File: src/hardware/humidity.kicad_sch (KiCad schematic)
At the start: 2 parts

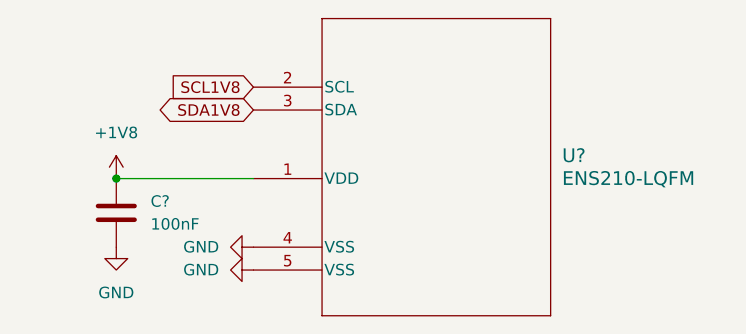
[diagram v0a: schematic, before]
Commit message: Added I²C Addresses
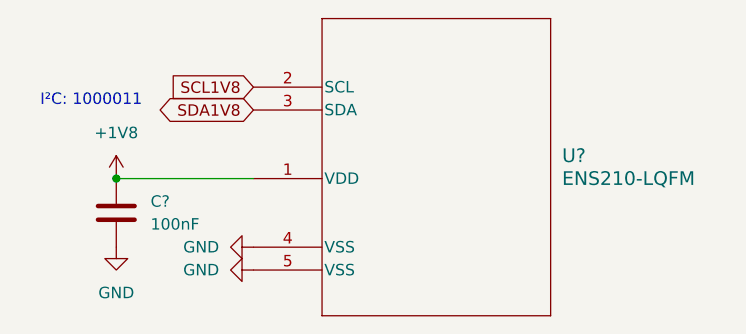
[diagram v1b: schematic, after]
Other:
- note added: "I²C: 1000011"
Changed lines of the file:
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@@
 		(date "2026-10-21")
+	)
+	(text "I²C: 1000011"
+		(exclude_from_sim no)
+		(at 116.586 95.504 0)
+		(effects
+			(font
+				(size 1.27 1.27)
+			)
+		)
 	)
 	(junction

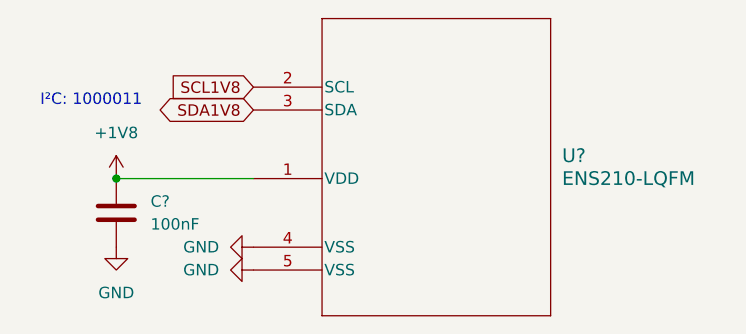
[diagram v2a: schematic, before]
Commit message: Replaced schematics, 3d models and footprints. Added vibration motor.
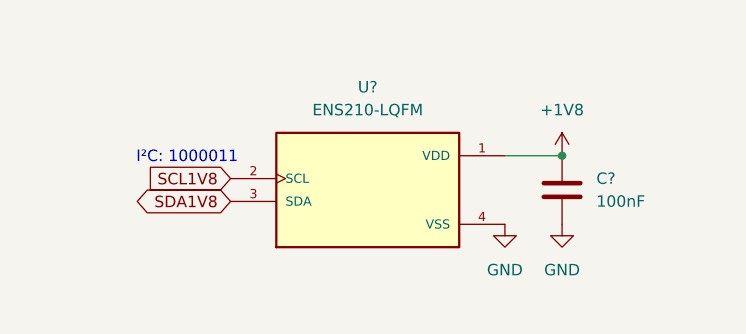
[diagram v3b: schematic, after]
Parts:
- removed U?: ENS210-LQFM, SON-04-ENS210_2X2_AMS, symbol ENS210-LQFM:ENS210-LQFM
- added U?: ENS210-LQFM, ENS210-LQFM:XDCR_ENS210-LQFM, symbol ENS210-LQFM:ENS210-LQFM
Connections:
- net +1V8: now also U?.1 (VDD)
- net GND: now also U?.4 (VSS), U?.5 (VSS)
- net SCL1V8: now also U?.2 (SCL)
- net SDA1V8: now also U?.3 (SDA)
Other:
- moved on the sheet: C?

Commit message: Cleanup & Fixes; Added footprints; Removed Light sensors
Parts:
- C56: renamed from C?; footprint (none) -> Capacitor_SMD:C_0603_1608Metric
- U18: renamed from U?; footprint ENS210-LQFM:XDCR_ENS210-LQFM -> Project:XDCR_ENS210-LQFM
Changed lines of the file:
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@@
 		(dnp no)
 		(fields_autoplaced yes)
-		(property "Reference" "#PWR0309"
+		(property "Reference" "#PWR0316"
 			(at 168.91 105.41 0)
 			(effects
@@
 			(project "raywatch"
 				(path "/7b654ee8-2a53-4d39-8b7d-32c7bb3cb0ed/bf067082-8f07-4e2a-8f09-1edc4b312956"
-					(reference "#PWR0309")
+					(reference "#PWR0316")
 					(unit 1)
 				)
@@
 		(dnp no)
 		(fields_autoplaced yes)
-		(property "Reference" "U?"
+		(property "Reference" "U18"
 			(at 147.32 93.98 0)
 			(effects
@@
 			)
 		)
-		(property "Footprint" "ENS210-LQFM:XDCR_ENS210-LQFM"
+		(property "Footprint" "Project:XDCR_ENS210-LQFM"
 			(at 147.32 104.14 0)
 			(effects
@@
 			(project "raywatch"
 				(path "/7b654ee8-2a53-4d39-8b7d-32c7bb3cb0ed/bf067082-8f07-4e2a-8f09-1edc4b312956"
-					(reference "U?")
+					(reference "U18")
 					(unit 1)
 				)
@@
 		(dnp no)
 		(fields_autoplaced yes)
-		(property "Reference" "#PWR0307"
+		(property "Reference" "#PWR0315"
 			(at 162.56 115.57 0)
 			(effects
@@
 			(project "raywatch"
 				(path "/7b654ee8-2a53-4d39-8b7d-32c7bb3cb0ed/bf067082-8f07-4e2a-8f09-1edc4b312956"
-					(reference "#PWR0307")
+					(reference "#PWR0315")
 					(unit 1)
 				)
@@
 		(dnp no)
 		(fields_autoplaced yes)
-		(property "Reference" "C?"
+		(property "Reference" "C56"
 			(at 172.72 104.1399 0)
 			(effects
@@
 			)
 		)
-		(property "Footprint" ""
+		(property "Footprint" "Capacitor_SMD:C_0603_1608Metric"
 			(at 169.8752 109.22 0)
 			(effects
@@
 			(project "raywatch"
 				(path "/7b654ee8-2a53-4d39-8b7d-32c7bb3cb0ed/bf067082-8f07-4e2a-8f09-1edc4b312956"
-					(reference "C?")
+					(reference "C56")
 					(unit 1)
 				)
@@
 		(dnp no)
 		(fields_autoplaced yes)
-		(property "Reference" "#PWR0310"
+		(property "Reference" "#PWR0317"
 			(at 168.91 115.57 0)
 			(effects
@@
 			(project "raywatch"
 				(path "/7b654ee8-2a53-4d39-8b7d-32c7bb3cb0ed/bf067082-8f07-4e2a-8f09-1edc4b312956"
-					(reference "#PWR0310")
+					(reference "#PWR0317")
 					(unit 1)
 				)

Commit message: Cleanup & Fixes; Changed GPIO; Added Camera; Added Microphone
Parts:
- renumbered C56 to C54
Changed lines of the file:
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@@
 		(dnp no)
 		(fields_autoplaced yes)
-		(property "Reference" "#PWR0316"
+		(property "Reference" "#PWR0312"
 			(at 168.91 105.41 0)
 			(effects
@@
 			(project "raywatch"
 				(path "/7b654ee8-2a53-4d39-8b7d-32c7bb3cb0ed/bf067082-8f07-4e2a-8f09-1edc4b312956"
-					(reference "#PWR0316")
+					(reference "#PWR0312")
 					(unit 1)
 				)
@@
 		(dnp no)
 		(fields_autoplaced yes)
-		(property "Reference" "#PWR0315"
+		(property "Reference" "#PWR0311"
 			(at 162.56 115.57 0)
 			(effects
@@
 			(project "raywatch"
 				(path "/7b654ee8-2a53-4d39-8b7d-32c7bb3cb0ed/bf067082-8f07-4e2a-8f09-1edc4b312956"
-					(reference "#PWR0315")
+					(reference "#PWR0311")
 					(unit 1)
 				)
@@
 		(dnp no)
 		(fields_autoplaced yes)
-		(property "Reference" "C56"
+		(property "Reference" "C54"
 			(at 172.72 104.1399 0)
 			(effects
@@
 			(project "raywatch"
 				(path "/7b654ee8-2a53-4d39-8b7d-32c7bb3cb0ed/bf067082-8f07-4e2a-8f09-1edc4b312956"
-					(reference "C56")
+					(reference "C54")
 					(unit 1)
 				)
@@
 		(dnp no)
 		(fields_autoplaced yes)
-		(property "Reference" "#PWR0317"
+		(property "Reference" "#PWR0313"
 			(at 168.91 115.57 0)
 			(effects
@@
 			(project "raywatch"
 				(path "/7b654ee8-2a53-4d39-8b7d-32c7bb3cb0ed/bf067082-8f07-4e2a-8f09-1edc4b312956"
-					(reference "#PWR0317")
+					(reference "#PWR0313")
 					(unit 1)
 				)

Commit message: Add Light Sensor and Proximity & Gesture Sensor; Changed GPIO
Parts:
- renumbered U18 to U19
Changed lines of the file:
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@@
 		(dnp no)
 		(fields_autoplaced yes)
-		(property "Reference" "#PWR0312"
+		(property "Reference" "#PWR0316"
 			(at 168.91 105.41 0)
 			(effects
@@
 			(project "raywatch"
 				(path "/7b654ee8-2a53-4d39-8b7d-32c7bb3cb0ed/bf067082-8f07-4e2a-8f09-1edc4b312956"
-					(reference "#PWR0312")
+					(reference "#PWR0316")
 					(unit 1)
 				)
@@
 		(dnp no)
 		(fields_autoplaced yes)
-		(property "Reference" "U18"
+		(property "Reference" "U19"
 			(at 147.32 93.98 0)
 			(effects
@@
 			(project "raywatch"
 				(path "/7b654ee8-2a53-4d39-8b7d-32c7bb3cb0ed/bf067082-8f07-4e2a-8f09-1edc4b312956"
-					(reference "U18")
+					(reference "U19")
 					(unit 1)
 				)
@@
 		(dnp no)
 		(fields_autoplaced yes)
-		(property "Reference" "#PWR0311"
+		(property "Reference" "#PWR0315"
 			(at 162.56 115.57 0)
 			(effects
@@
 			(project "raywatch"
 				(path "/7b654ee8-2a53-4d39-8b7d-32c7bb3cb0ed/bf067082-8f07-4e2a-8f09-1edc4b312956"
-					(reference "#PWR0311")
+					(reference "#PWR0315")
 					(unit 1)
 				)
@@
 		(dnp no)
 		(fields_autoplaced yes)
-		(property "Reference" "#PWR0313"
+		(property "Reference" "#PWR0317"
 			(at 168.91 115.57 0)
 			(effects
@@
 			(project "raywatch"
 				(path "/7b654ee8-2a53-4d39-8b7d-32c7bb3cb0ed/bf067082-8f07-4e2a-8f09-1edc4b312956"
-					(reference "#PWR0313")
+					(reference "#PWR0317")
 					(unit 1)
 				)

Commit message: Changed footprints from 0603 to 0402
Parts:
- C54: footprint Capacitor_SMD:C_0603_1608Metric -> Capacitor_SMD:C_0504_1310Metric
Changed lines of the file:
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@@
 			)
 		)
-		(property "Footprint" "Capacitor_SMD:C_0603_1608Metric"
+		(property "Footprint" "Capacitor_SMD:C_0504_1310Metric"
 			(at 169.8752 109.22 0)
 			(effects
